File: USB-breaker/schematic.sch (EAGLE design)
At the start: 16 parts, among them K1 G6K-2P, K3 G6K-2P, X1 PN87520-S, X2 PN87520-S

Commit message: Renamed some nets
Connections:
- net D+-IN renamed D+_IN
- net D+-OUT renamed D+_OUT
- net D--IN renamed D-_IN
- net D--OUT renamed D-_OUT
- net GND-IN renamed GND_IN
- net N$1 renamed GND_OUT
- net VCC-IN renamed VCC_IN
- net VCC-OUT renamed VCC_OUT
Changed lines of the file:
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@@
 <layer number="48" name="Document" color="7" fill="1" visible="no" active="no"/>
 <layer number="49" name="Reference" color="7" fill="1" visible="no" active="no"/>
+<layer number="50" name="dxf" color="7" fill="1" visible="no" active="no"/>
 <layer number="51" name="tDocu" color="7" fill="1" visible="no" active="no"/>
 <layer number="52" name="bDocu" color="7" fill="1" visible="no" active="no"/>
+<layer number="53" name="tGND_GNDA" color="7" fill="9" visible="no" active="no"/>
+<layer number="54" name="bGND_GNDA" color="1" fill="9" visible="no" active="no"/>
+<layer number="56" name="wert" color="7" fill="1" visible="no" active="no"/>
 <layer number="91" name="Nets" color="2" fill="1" visible="yes" active="yes"/>
 <layer number="92" name="Busses" color="1" fill="1" visible="yes" active="yes"/>
@@
 <layer number="98" name="Guide" color="6" fill="1" visible="yes" active="yes"/>
 <layer number="99" name="SpiceOrder" color="5" fill="1" visible="yes" active="yes"/>
+<layer number="100" name="Muster" color="7" fill="1" visible="no" active="no"/>
+<layer number="101" name="Patch_Top" color="12" fill="4" visible="yes" active="yes"/>
+<layer number="102" name="Vscore" color="7" fill="1" visible="yes" active="yes"/>
+<layer number="103" name="tMap" color="7" fill="1" visible="yes" active="yes"/>
+<layer number="104" name="Name" color="16" fill="1" visible="yes" active="yes"/>
+<layer number="105" name="tPlate" color="7" fill="1" visible="yes" active="yes"/>
+<layer number="106" name="bPlate" color="7" fill="1" visible="yes" active="yes"/>
+<layer number="107" name="Crop" color="7" fill="1" visible="yes" active="yes"/>
+<layer number="108" name="tplace-old" color="10" fill="1" visible="no" active="yes"/>
+<layer number="109" name="ref-old" color="11" fill="1" visible="no" active="yes"/>
+<layer number="116" name="Patch_BOT" color="9" fill="4" visible="yes" active="yes"/>
+<layer number="121" name="_tsilk" color="7" fill="1" visible="yes" active="yes"/>
+<layer number="122" name="_bsilk" color="7" fill="1" visible="yes" active="yes"/>
+<layer number="125" name="_tNames" color="7" fill="1" visible="yes" active="yes"/>
+<layer number="144" name="Drill_legend" color="7" fill="1" visible="yes" active="yes"/>
+<layer number="151" name="HeatSink" color="7" fill="1" visible="yes" active="yes"/>
+<layer number="199" name="Contour" color="7" fill="1" visible="yes" active="yes"/>
+<layer number="200" name="200bmp" color="1" fill="10" visible="yes" active="yes"/>
+<layer number="201" name="201bmp" color="2" fill="10" visible="yes" active="yes"/>
+<layer number="202" name="202bmp" color="3" fill="10" visible="yes" active="yes"/>
+<layer number="203" name="203bmp" color="4" fill="10" visible="yes" active="yes"/>
+<layer number="204" name="204bmp" color="5" fill="10" visible="yes" active="yes"/>
+<layer number="205" name="205bmp" color="6" fill="10" visible="yes" active="yes"/>
+<layer number="206" name="206bmp" color="7" fill="10" visible="yes" active="yes"/>
+<layer number="207" name="207bmp" color="8" fill="10" visible="yes" active="yes"/>
+<layer number="208" name="208bmp" color="9" fill="10" visible="yes" active="yes"/>
+<layer number="209" name="209bmp" color="7" fill="1" visible="yes" active="yes"/>
+<layer number="210" name="210bmp" color="7" fill="1" visible="yes" active="yes"/>
+<layer number="211" name="211bmp" color="7" fill="1" visible="yes" active="yes"/>
+<layer number="212" name="212bmp" color="7" fill="1" visible="yes" active="yes"/>
+<layer number="213" name="213bmp" color="7" fill="1" visible="yes" active="yes"/>
+<layer number="214" name="214bmp" color="7" fill="1" visible="yes" active="yes"/>
+<layer number="215" name="215bmp" color="7" fill="1" visible="yes" active="yes"/>
+<layer number="216" name="216bmp" color="7" fill="1" visible="yes" active="yes"/>
+<layer number="217" name="217bmp" color="18" fill="1" visible="no" active="no"/>
+<layer number="218" name="218bmp" color="19" fill="1" visible="no" active="no"/>
+<layer number="219" name="219bmp" color="20" fill="1" visible="no" active="no"/>
+<layer number="220" name="220bmp" color="21" fill="1" visible="no" active="no"/>
+<layer number="221" name="221bmp" color="22" fill="1" visible="no" active="no"/>
+<layer number="222" name="222bmp" color="23" fill="1" visible="no" active="no"/>
+<layer number="223" name="223bmp" color="24" fill="1" visible="no" active="no"/>
+<layer number="224" name="224bmp" color="25" fill="1" visible="no" active="no"/>
+<layer number="250" name="Descript" color="3" fill="1" visible="no" active="no"/>
+<layer number="251" name="SMDround" color="12" fill="11" visible="no" active="no"/>
+<layer number="254" name="cooling" color="7" fill="1" visible="yes" active="yes"/>
 </layers>
 <schematic xreflabel="%F%N/%S.%C%R" xrefpart="/%S.%C%R">
@@
 </busses>
 <nets>
-<net name="VCC-IN" class="0">
+<net name="VCC_IN" class="0">
 <segment>
 <wire x1="109.22" y1="111.76" x2="109.22" y2="109.22" width="0.1524" layer="91"/>
@@
 </segment>
 </net>
-<net name="GND-IN" class="0">
+<net name="GND_IN" class="0">
 <segment>
 <wire x1="116.84" y1="111.76" x2="116.84" y2="101.6" width="0.1524" layer="91"/>
@@
 </segment>
 </net>
-<net name="VCC-OUT" class="0">
+<net name="VCC_OUT" class="0">
 <segment>
 <wire x1="104.14" y1="35.56" x2="162.56" y2="35.56" width="0.1524" layer="91"/>
@@
 </segment>
 </net>
-<net name="D--IN" class="0">
+<net name="D-_IN" class="0">
 <segment>
 <wire x1="111.76" y1="111.76" x2="111.76" y2="106.68" width="0.1524" layer="91"/>
@@
 </segment>
 </net>
-<net name="D+-IN" class="0">
+<net name="D+_IN" class="0">
 <segment>
 <wire x1="114.3" y1="111.76" x2="114.3" y2="104.14" width="0.1524" layer="91"/>
@@
 </segment>
 </net>
-<net name="D+-OUT" class="0">
+<net name="D+_OUT" class="0">
 <segment>
 <wire x1="60.96" y1="40.64" x2="162.56" y2="40.64" width="0.1524" layer="91"/>
@@
 </segment>
 </net>
-<net name="D--OUT" class="0">
+<net name="D-_OUT" class="0">
 <segment>
 <wire x1="45.72" y1="38.1" x2="162.56" y2="38.1" width="0.1524" layer="91"/>
@@
 </segment>
 </net>
-<net name="N$1" class="0">
+<net name="GND_OUT" class="0">
 <segment>
 <pinref part="X2" gate="G$1" pin="4"/>

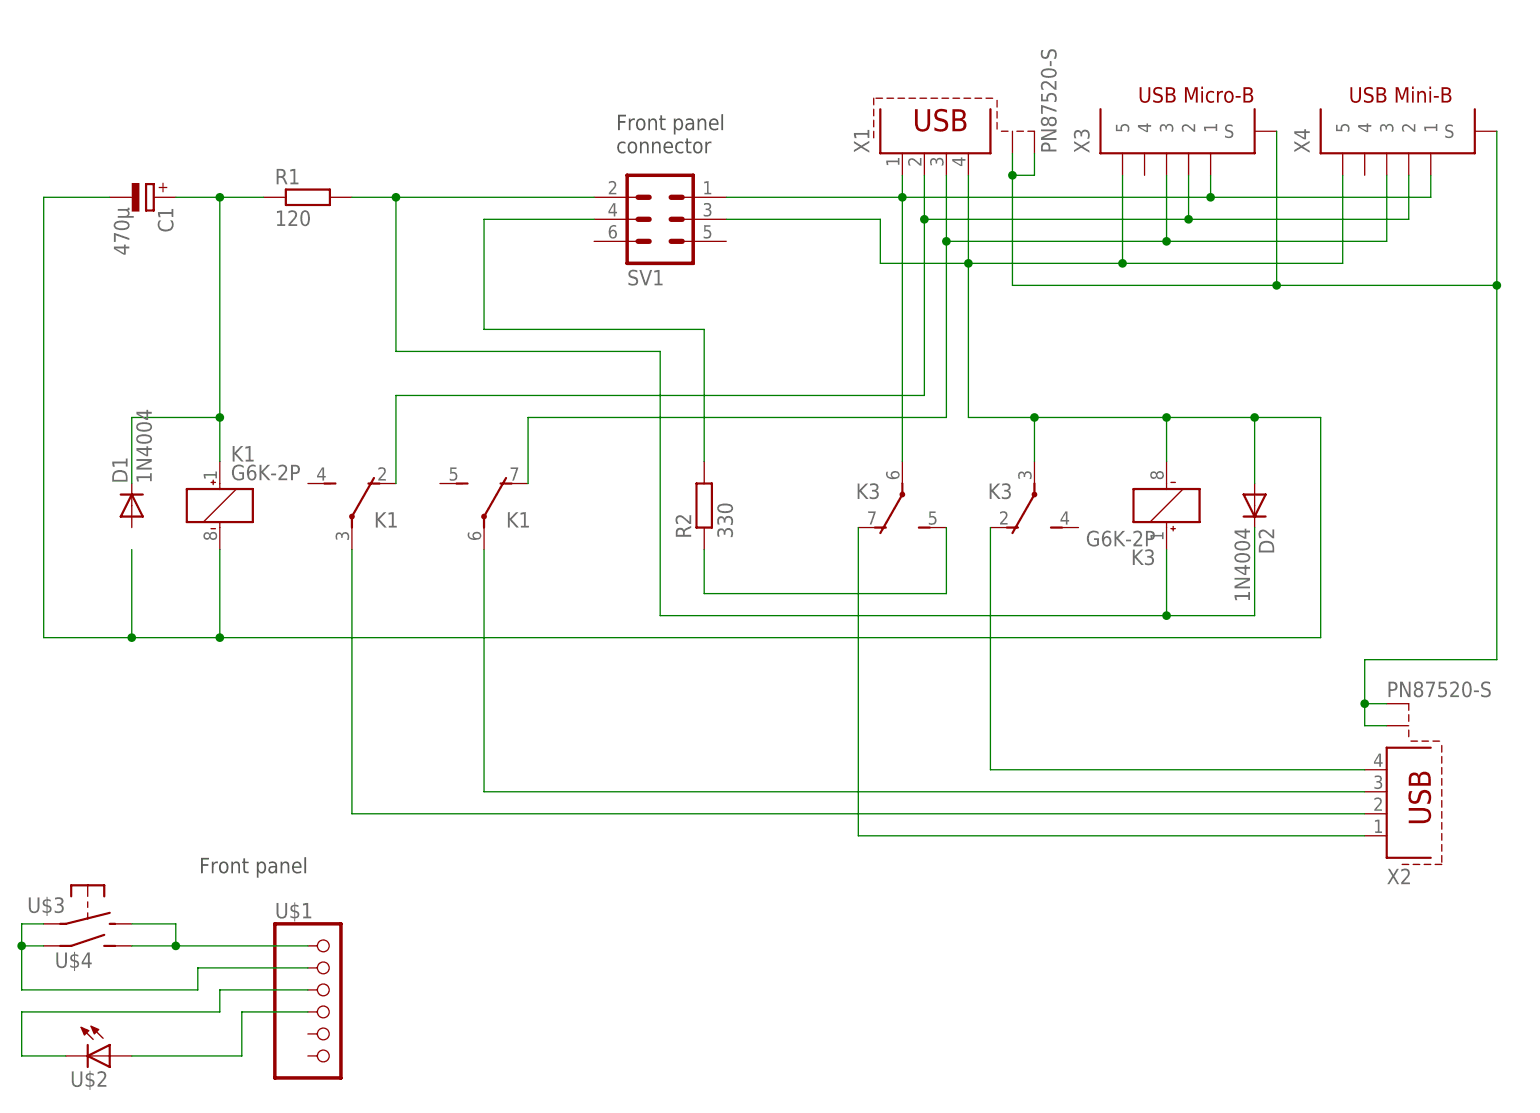
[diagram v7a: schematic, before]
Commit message: New external control interface as pin header.
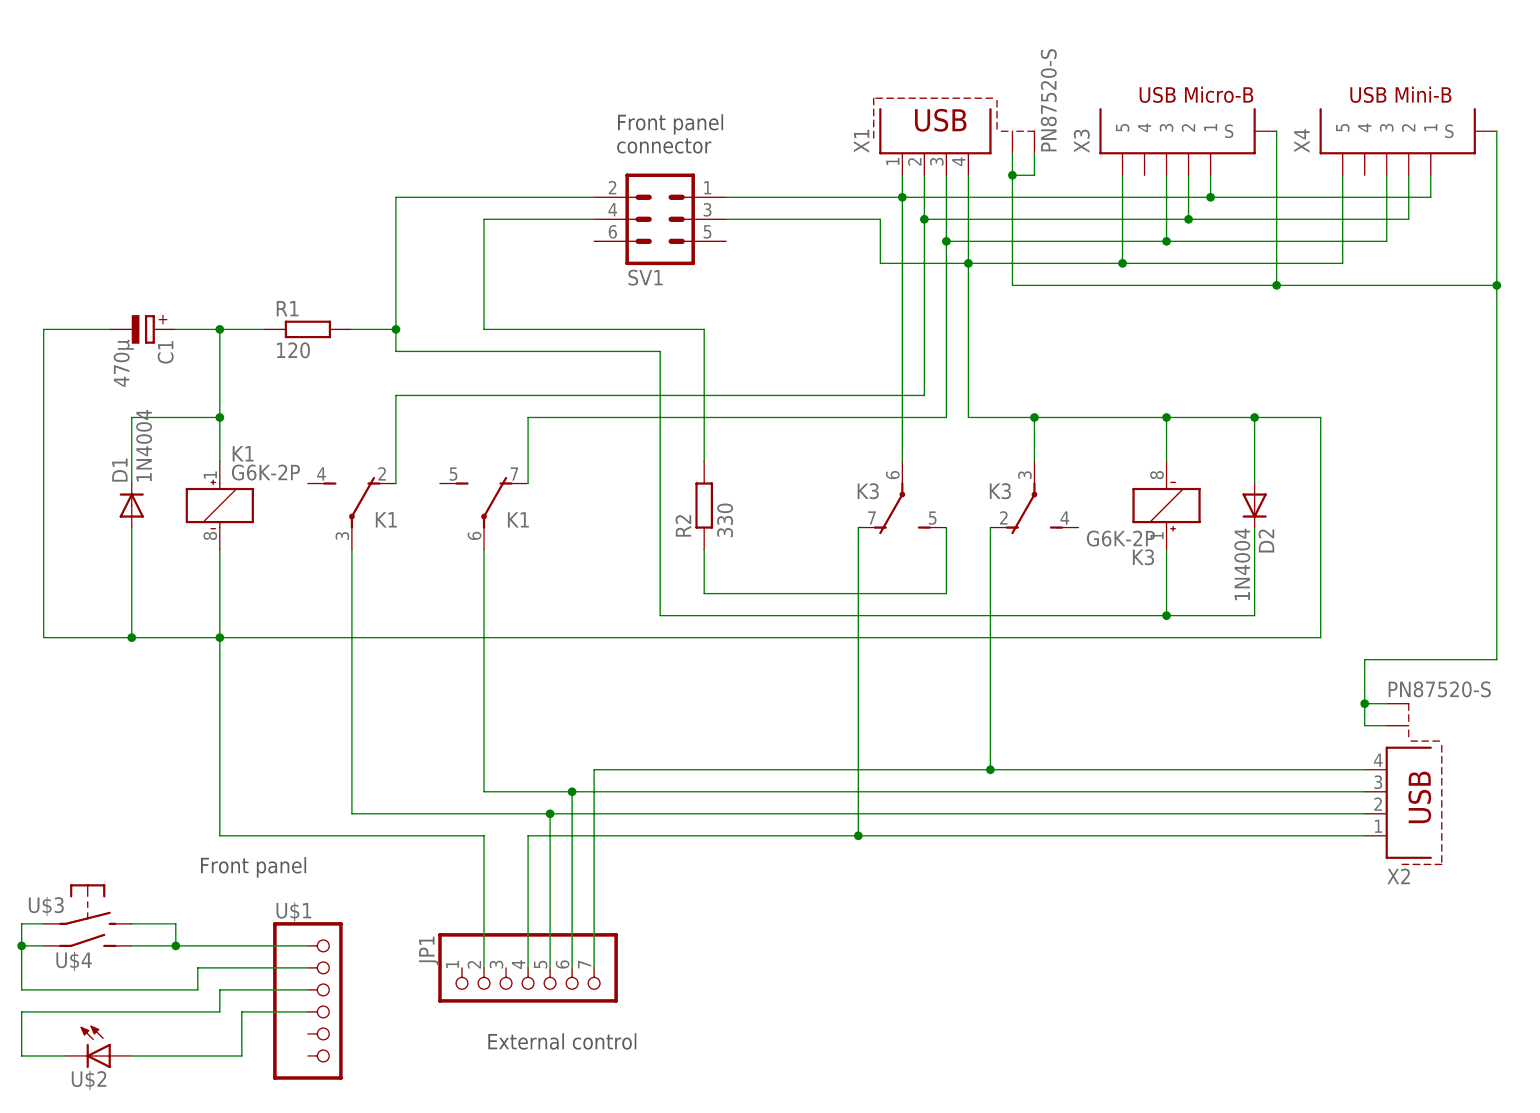
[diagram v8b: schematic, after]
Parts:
- added JP1: (no value), pinhead:PINHD-1X7/90
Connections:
- net D+_OUT: now also JP1.6
- net D-_OUT: now also JP1.5
- net GND_IN: now also D1.A, JP1.2
- net GND_OUT: now also JP1.7
- net VCC_OUT: now also JP1.4
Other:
- note added: "External control"
- moved on the sheet: C1, R1
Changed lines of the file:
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@@
 <layer number="97" name="Info" color="7" fill="1" visible="yes" active="yes"/>
 <layer number="98" name="Guide" color="6" fill="1" visible="yes" active="yes"/>
-<layer number="99" name="SpiceOrder" color="5" fill="1" visible="yes" active="yes"/>
+<layer number="99" name="SpiceOrder" color="5" fill="1" visible="no" active="yes"/>
 <layer number="100" name="Muster" color="7" fill="1" visible="no" active="no"/>
 <layer number="101" name="Patch_Top" color="12" fill="4" visible="yes" active="yes"/>
@@
 <part name="U$3" library="mibe" deviceset="EXTERNAL_PUSH_BUTTON" device=""/>
 <part name="U$4" library="mibe" deviceset="EXTERNAL_SWITCH" device=""/>
+<part name="JP1" library="pinhead" deviceset="PINHD-1X7" device="/90"/>
 </parts>
 <sheets>
@@
 <text x="76.2" y="114.3" size="1.778" layer="97">Front panel
 connector</text>
+<text x="78.74" y="12.7" size="1.778" layer="97" rot="R180">External control</text>
 </plain>
 <instances>
 <instance part="FRAME1" gate="G$1" x="0" y="0"/>
-<instance part="R1" gate="G$1" x="40.64" y="109.22"/>
-<instance part="C1" gate="G$1" x="22.86" y="109.22" rot="R270"/>
+<instance part="R1" gate="G$1" x="40.64" y="93.98"/>
+<instance part="C1" gate="G$1" x="22.86" y="93.98" rot="R270"/>
 <instance part="D1" gate="1" x="20.32" y="73.66" rot="R90"/>
 <instance part="R2" gate="G$1" x="86.36" y="73.66" rot="R90"/>
@@
 <attribute name="NAME" x="11.43" y="20.32" size="1.778" layer="95"/>
 </instance>
+<instance part="JP1" gate="A" x="66.04" y="17.78" rot="MR270"/>
 </instances>
 <busses>
@@
 <pinref part="K1" gate="1" pin="-"/>
 <wire x1="30.48" y1="68.58" x2="30.48" y2="58.42" width="0.1524" layer="91"/>
+<junction x="30.48" y="58.42"/>
 <wire x1="30.48" y1="58.42" x2="20.32" y2="58.42" width="0.1524" layer="91"/>
-<junction x="30.48" y="58.42"/>
-<wire x1="20.32" y1="68.58" x2="20.32" y2="58.42" width="0.1524" layer="91"/>
 <wire x1="20.32" y1="58.42" x2="10.16" y2="58.42" width="0.1524" layer="91"/>
-<wire x1="10.16" y1="58.42" x2="10.16" y2="109.22" width="0.1524" layer="91"/>
+<wire x1="10.16" y1="58.42" x2="10.16" y2="93.98" width="0.1524" layer="91"/>
+<pinref part="C1" gate="G$1" pin="-"/>
+<wire x1="10.16" y1="93.98" x2="17.78" y2="93.98" width="0.1524" layer="91"/>
+<pinref part="JP1" gate="A" pin="2"/>
+<wire x1="60.96" y1="20.32" x2="60.96" y2="35.56" width="0.1524" layer="91"/>
+<wire x1="60.96" y1="35.56" x2="30.48" y2="35.56" width="0.1524" layer="91"/>
+<wire x1="30.48" y1="35.56" x2="30.48" y2="58.42" width="0.1524" layer="91"/>
+<pinref part="D1" gate="1" pin="A"/>
+<wire x1="20.32" y1="71.12" x2="20.32" y2="58.42" width="0.1524" layer="91"/>
 <junction x="20.32" y="58.42"/>
-<pinref part="C1" gate="G$1" pin="-"/>
-<wire x1="10.16" y1="109.22" x2="17.78" y2="109.22" width="0.1524" layer="91"/>
 </segment>
 <segment>
@@
 <pinref part="K3" gate="3" pin="O"/>
 <pinref part="X2" gate="G$1" pin="1"/>
+<pinref part="JP1" gate="A" pin="4"/>
+<wire x1="104.14" y1="35.56" x2="66.04" y2="35.56" width="0.1524" layer="91"/>
+<wire x1="66.04" y1="35.56" x2="66.04" y2="20.32" width="0.1524" layer="91"/>
+<junction x="104.14" y="35.56"/>
 </segment>
 </net>
@@
 <net name="D+_OUT" class="0">
 <segment>
-<wire x1="60.96" y1="40.64" x2="162.56" y2="40.64" width="0.1524" layer="91"/>
+<wire x1="60.96" y1="40.64" x2="71.12" y2="40.64" width="0.1524" layer="91"/>
 <pinref part="K1" gate="3" pin="P"/>
+<wire x1="71.12" y1="40.64" x2="162.56" y2="40.64" width="0.1524" layer="91"/>
 <wire x1="60.96" y1="68.58" x2="60.96" y2="40.64" width="0.1524" layer="91"/>
 <pinref part="X2" gate="G$1" pin="3"/>
+<pinref part="JP1" gate="A" pin="6"/>
+<wire x1="71.12" y1="20.32" x2="71.12" y2="40.64" width="0.1524" layer="91"/>
+<junction x="71.12" y="40.64"/>
 </segment>
 </net>
 <net name="D-_OUT" class="0">
 <segment>
-<wire x1="45.72" y1="38.1" x2="162.56" y2="38.1" width="0.1524" layer="91"/>
+<wire x1="45.72" y1="38.1" x2="68.58" y2="38.1" width="0.1524" layer="91"/>
 <pinref part="K1" gate="2" pin="P"/>
+<wire x1="68.58" y1="38.1" x2="162.56" y2="38.1" width="0.1524" layer="91"/>
 <wire x1="45.72" y1="68.58" x2="45.72" y2="38.1" width="0.1524" layer="91"/>
 <pinref part="X2" gate="G$1" pin="2"/>
+<pinref part="JP1" gate="A" pin="5"/>
+<wire x1="68.58" y1="20.32" x2="68.58" y2="38.1" width="0.1524" layer="91"/>
+<junction x="68.58" y="38.1"/>
 </segment>
 </net>
@@
 <pinref part="R1" gate="G$1" pin="1"/>
 <pinref part="C1" gate="G$1" pin="+"/>
-<wire x1="35.56" y1="109.22" x2="30.48" y2="109.22" width="0.1524" layer="91"/>
-<wire x1="30.48" y1="109.22" x2="25.4" y2="109.22" width="0.1524" layer="91"/>
+<wire x1="35.56" y1="93.98" x2="30.48" y2="93.98" width="0.1524" layer="91"/>
+<wire x1="30.48" y1="93.98" x2="25.4" y2="93.98" width="0.1524" layer="91"/>
 <wire x1="30.48" y1="78.74" x2="30.48" y2="83.82" width="0.1524" layer="91"/>
-<junction x="30.48" y="109.22"/>
-<wire x1="30.48" y1="83.82" x2="30.48" y2="109.22" width="0.1524" layer="91"/>
+<junction x="30.48" y="93.98"/>
+<wire x1="30.48" y1="83.82" x2="30.48" y2="93.98" width="0.1524" layer="91"/>
 <wire x1="30.48" y1="83.82" x2="20.32" y2="83.82" width="0.1524" layer="91"/>
 <junction x="30.48" y="83.82"/>
@@
 <segment>
 <pinref part="R1" gate="G$1" pin="2"/>
-<wire x1="50.8" y1="109.22" x2="45.72" y2="109.22" width="0.1524" layer="91"/>
-<wire x1="50.8" y1="109.22" x2="50.8" y2="91.44" width="0.1524" layer="91"/>
+<wire x1="50.8" y1="93.98" x2="45.72" y2="93.98" width="0.1524" layer="91"/>
+<wire x1="50.8" y1="93.98" x2="50.8" y2="91.44" width="0.1524" layer="91"/>
 <wire x1="50.8" y1="91.44" x2="81.28" y2="91.44" width="0.1524" layer="91"/>
 <wire x1="81.28" y1="91.44" x2="81.28" y2="60.96" width="0.1524" layer="91"/>
@@
 <pinref part="SV1" gate="1" pin="2"/>
 <wire x1="73.66" y1="109.22" x2="50.8" y2="109.22" width="0.1524" layer="91"/>
-<junction x="50.8" y="109.22"/>
+<wire x1="50.8" y1="109.22" x2="50.8" y2="93.98" width="0.1524" layer="91"/>
+<junction x="50.8" y="93.98"/>
 </segment>
 <segment>
@@
 <pinref part="K3" gate="2" pin="O"/>
 <wire x1="119.38" y1="71.12" x2="119.38" y2="43.18" width="0.1524" layer="91"/>
-</segment>
-</net>
+<pinref part="JP1" gate="A" pin="7"/>
+<wire x1="119.38" y1="43.18" x2="73.66" y2="43.18" width="0.1524" layer="91"/>
+<wire x1="73.66" y1="43.18" x2="73.66" y2="20.32" width="0.1524" layer="91"/>
+<junction x="119.38" y="43.18"/>
+</segment>
+</net>
